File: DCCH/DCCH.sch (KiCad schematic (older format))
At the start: 56 parts, among them J1 Conn_01x02, J2 Conn_01x02, J211 Conn_01x02, J212 Conn_01x02, J221 Conn_01x02, J222 Conn_01x02, J231 Conn_01x02, J232 Conn_01x02, J241 Conn_01x02, J242 Conn_01x02, J3 Conn_02x04_Odd_Even, J4 Conn_02x04_Odd_Even, U11 SN74HC595, U12 SN74HC595, U13 SN74HC595, U14 SN74HC595, U21 SN754410, U22 SN754410, U23 SN754410, U24 SN754410

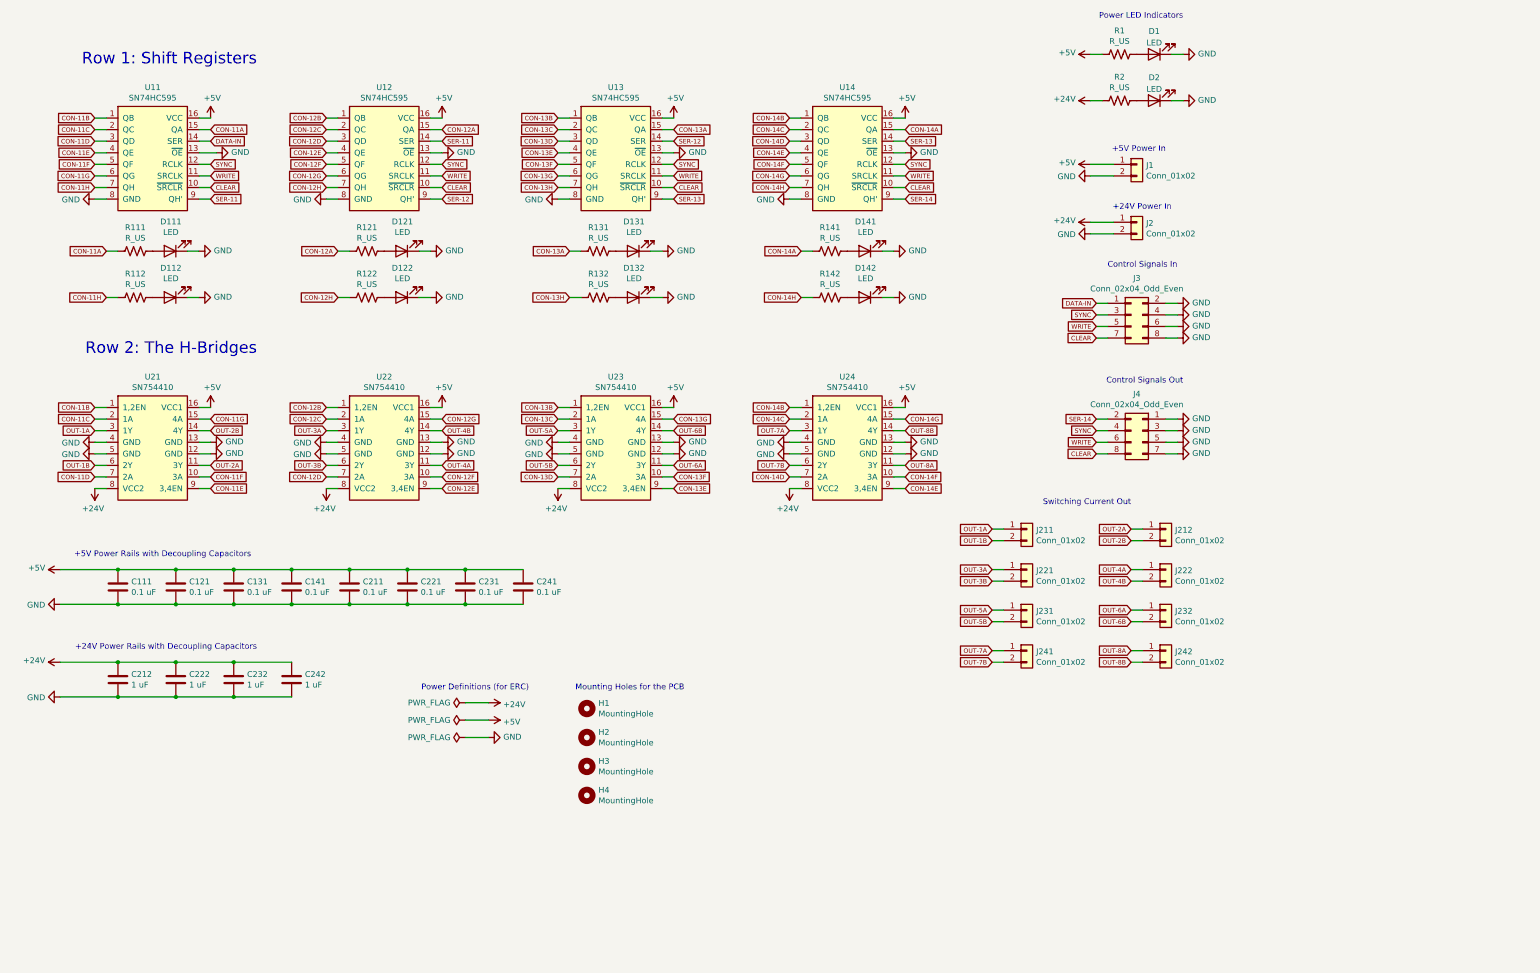
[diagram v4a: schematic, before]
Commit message: Dean completely overhauled the board. Updated board and schematics
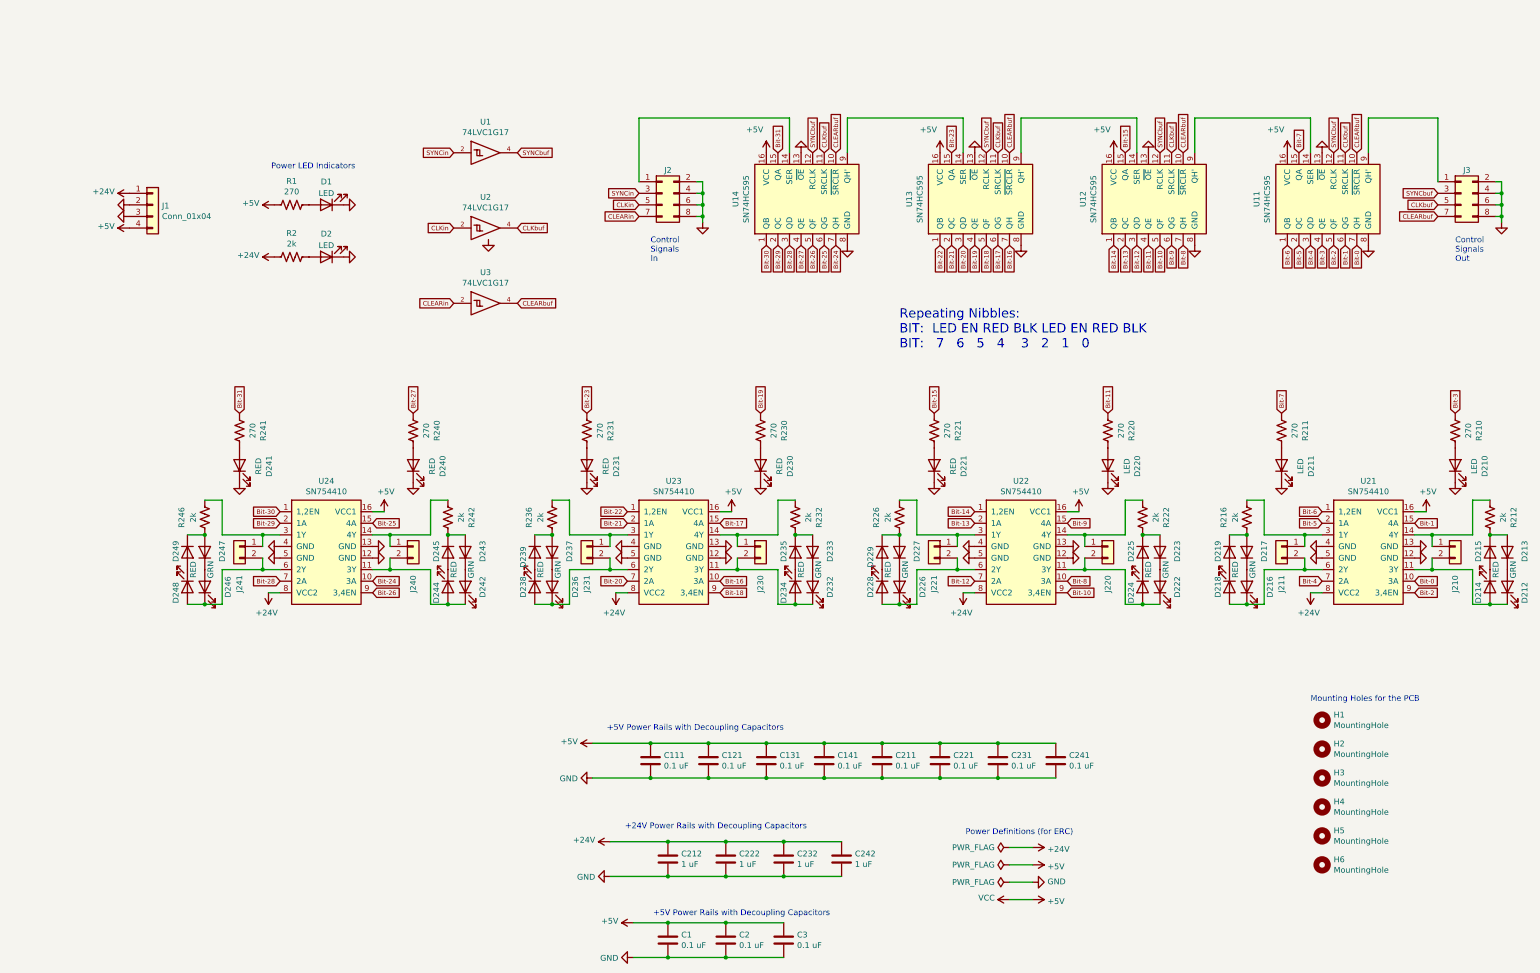
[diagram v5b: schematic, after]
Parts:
- removed J1, J2: Conn_01x02, Connector_Phoenix_MC:PhoenixContact_MC_1,5_2-GF-3.5_1x02_P3.50mm_Horizontal_ThreadedFlange_MountHole, symbol Connector_Generic:Conn_01x02
- added C1, C2, C3: 0.1 uF, Capacitor_SMD:C_0805_2012Metric, symbol Device:C
- added D212, D216, D222, D226, D232, D236, D242, D246: GRN, LED_SMD:LED_0805_2012Metric, symbol Device:LED
- added D213, D215, D217, D219, D223, D225, D227, D229, D233, D235, D237, D239, D243, D245, D247, D249: 1N4148W, Diode_SMD:D_SOD-123, symbol Diode:1N4148W
- added D214, D218, D224, D228, D234, D238, D244, D248: RED, LED_SMD:LED_0805_2012Metric, symbol Device:LED
- added H5, H6: MountingHole, MountingHole:MountingHole_3.5mm, symbol Mechanical:MountingHole
- added J1: Conn_01x04, Connector_Phoenix_MC:PhoenixContact_MC_1,5_4-GF-3.5_1x04_P3.50mm_Horizontal_ThreadedFlange_MountHole, symbol Connector_Generic:Conn_01x04
- added R212, R216, R222, R226, R232, R236, R242, R246: 2k, Resistor_SMD:R_0805_2012Metric, symbol Device:R_US
- added U1, U2, U3: 74LVC1G17, Package_TO_SOT_SMD:SOT-23-5_HandSoldering, symbol 74xGxx:74LVC1G17
- D221: renamed from D131; value LED -> RED
- D230: renamed from D122; value LED -> RED
- D231: renamed from D121; value LED -> RED
- D240: renamed from D112; value LED -> RED
- D241: renamed from D111; value LED -> RED
- J2: renamed from J3; footprint Connector_PinHeader_2.54mm:PinHeader_2x04_P2.54mm_Vertical -> Connector_IDC:IDC-Header_2x04_P2.54mm_Vertical
- J3: renamed from J4; footprint Connector_PinHeader_2.54mm:PinHeader_2x04_P2.54mm_Vertical -> Connector_IDC:IDC-Header_2x04_P2.54mm_Vertical
- R1: value R_US -> 270
- R2: value R_US -> 2k
- R210: renamed from R142; value R_US -> 270
- R211: renamed from R141; value R_US -> 270
- R220: renamed from R132; value R_US -> 270
- R221: renamed from R131; value R_US -> 270
- R230: renamed from R122; value R_US -> 270
- R231: renamed from R121; value R_US -> 270
- R240: renamed from R112; value R_US -> 270
- R241: renamed from R111; value R_US -> 270
- renumbered D142 to D210, D141 to D211, D132 to D220, J242 to J210, J241 to J211, J232 to J220, J231 to J221, J222 to J230, J221 to J231, J212 to J240, J211 to J241, U14 to U11, U13 to U12, U12 to U13, U11 to U14, U24 to U21, U23 to U22, U22 to U23, U21 to U24
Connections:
- net +24V: now also J1.1 (Pin_1)
- net +5V: now also C1.1, C2.1, C3.1, J1.4 (Pin_4), U1.5 (VCC), U2.5 (VCC), U3.5 (VCC)
- net GND: now also J3.2 (Pin_2), J3.4 (Pin_4), J3.6 (Pin_6), J3.8 (Pin_8), C1.2, C2.2, C3.2, J1.2 (Pin_2), J1.3 (Pin_3), U1.3 (GND), U2.3 (GND), U3.3 (GND); no longer J3.1 (Pin_1), J3.3 (Pin_3), J3.5 (Pin_5), J3.7 (Pin_7)
- net CLEAR renamed CLEARbuf
- net CLEARbuf: now also J3.7 (Pin_7), U3.4; no longer J2.7 (Pin_7), J3.8 (Pin_8)
- net CON-11A renamed Bit-31
- net CON-11B renamed Bit-30
- net CON-11C renamed Bit-29
- net CON-11D renamed Bit-28
- net CON-11E renamed Bit-26
- net Bit-26: now also U14.5 (QF); no longer U14.4 (QE)
- net CON-11F renamed Bit-24
- net Bit-24: now also U14.7 (QH); no longer U14.5 (QF)
- net CON-11G renamed Bit-25
- net CON-11H renamed Bit-27
- net Bit-27: now also U14.4 (QE); no longer U14.7 (QH)
- net CON-12A renamed Bit-23
- net CON-12B renamed Bit-22
- net CON-12C renamed Bit-21
- net CON-12D renamed Bit-20
- net CON-12E renamed Bit-18
- net Bit-18: now also U13.5 (QF); no longer U13.4 (QE)
- net CON-12F renamed Bit-16
- net Bit-16: now also U13.7 (QH); no longer U13.5 (QF)
- net CON-12G renamed Bit-17
- net CON-12H renamed Bit-19
- net Bit-19: now also U13.4 (QE); no longer U13.7 (QH)
- net CON-13A renamed Bit-15
- net CON-13B renamed Bit-14
- net CON-13C renamed Bit-13
- net CON-13D renamed Bit-12
- net CON-13E renamed Bit-10
- net Bit-10: now also U12.5 (QF); no longer U12.4 (QE)
- net CON-13F renamed Bit-8
- net Bit-8: now also U12.7 (QH); no longer U12.5 (QF)
- net CON-13G renamed Bit-9
- net CON-13H renamed Bit-11
- net Bit-11: now also U12.4 (QE); no longer U12.7 (QH)
- net CON-14A renamed Bit-7
- net CON-14B renamed Bit-6
- net CON-14C renamed Bit-5
- net CON-14D renamed Bit-4
- net CON-14E renamed Bit-2
- net Bit-2: now also U11.5 (QF); no longer U11.4 (QE)
- net CON-14F renamed Bit-0
- net Bit-0: now also U11.7 (QH); no longer U11.5 (QF)
- net CON-14G renamed Bit-1
- net CON-14H renamed Bit-3
- net Bit-3: now also U11.4 (QE); no longer U11.7 (QH)
- net DATA-IN: no longer names the net of J2.1 (Pin_1), U14.14 (SER)
- net OUT-1A: no longer names the net of J241.1 (Pin_1), U24.3 (1Y)
- net OUT-1A: now also R246.2
- net OUT-1B: no longer names the net of J241.2 (Pin_2), U24.6 (2Y)
- net OUT-1B: now also D246.1 (K), D248.2 (A)
- net OUT-2A: no longer names the net of U24.11 (3Y)
- net OUT-2A: now also J240.2 (Pin_2), D242.1 (K), D244.2 (A); no longer J240.1 (Pin_1)
- net OUT-2B: no longer names the net of U24.14 (4Y)
- net OUT-2B: now also J240.1 (Pin_1), R242.2; no longer J240.2 (Pin_2)
- net OUT-3A: no longer names the net of J231.1 (Pin_1), U23.3 (1Y)
- net OUT-3A: now also R236.2
- net OUT-3B: no longer names the net of J231.2 (Pin_2), U23.6 (2Y)
- net OUT-3B: now also D236.1 (K), D238.2 (A)
- net OUT-4A: no longer names the net of U23.11 (3Y)
- net OUT-4A: now also J230.2 (Pin_2), D232.1 (K), D234.2 (A); no longer J230.1 (Pin_1)
- net OUT-4B: no longer names the net of U23.14 (4Y)
- net OUT-4B: now also J230.1 (Pin_1), R232.2; no longer J230.2 (Pin_2)
- net OUT-5A: no longer names the net of J221.1 (Pin_1), U22.3 (1Y)
- net OUT-5A: now also R226.2
- net OUT-5B: no longer names the net of J221.2 (Pin_2), U22.6 (2Y)
- net OUT-5B: now also D226.1 (K), D228.2 (A)
- net OUT-6A: no longer names the net of U22.11 (3Y)
- net OUT-6A: now also J220.2 (Pin_2), D222.1 (K), D224.2 (A); no longer J220.1 (Pin_1)
- net OUT-6B: no longer names the net of U22.14 (4Y)
- net OUT-6B: now also J220.1 (Pin_1), R222.2; no longer J220.2 (Pin_2)
- net OUT-7A: no longer names the net of J211.1 (Pin_1), U21.3 (1Y)
- net OUT-7A: now also R216.2
- net OUT-7B: no longer names the net of J211.2 (Pin_2), U21.6 (2Y)
- net OUT-7B: now also D216.1 (K), D218.2 (A)
- net OUT-8A: no longer names the net of U21.11 (3Y)
- net OUT-8A: now also J210.2 (Pin_2), D212.1 (K), D214.2 (A); no longer J210.1 (Pin_1)
- net OUT-8B: no longer names the net of U21.14 (4Y)
- net OUT-8B: now also J210.1 (Pin_1), R212.2; no longer J210.2 (Pin_2)
- net SER-11: no longer names the net of U13.14 (SER), U14.9 (QH')
- net SER-12: no longer names the net of U12.14 (SER), U13.9 (QH')
- net SER-13: no longer names the net of U11.14 (SER), U12.9 (QH')
- net SER-14: no longer names the net of U11.9 (QH')
- net SER-14: now also J3.1 (Pin_1); no longer J3.2 (Pin_2)
- net SYNC renamed SYNCbuf
- net SYNCbuf: now also J3.3 (Pin_3), U1.4; no longer J2.3 (Pin_3), J3.4 (Pin_4)
- net WRITE renamed CLKbuf
- net CLKbuf: now also J3.5 (Pin_5), U2.4; no longer J2.5 (Pin_5), J3.6 (Pin_6)
- new net: D236.2 (A), D237.1 (K)
- new net: D237.2 (A), D239.1 (K), R236.1
- new net: D238.1 (K), D239.2 (A)
- new net: D242.2 (A), D243.1 (K)
- new net: D243.2 (A), D245.1 (K), R242.1
- new net: D244.1 (K), D245.2 (A)
- new net: D226.2 (A), D227.1 (K)
- new net: D227.2 (A), D229.1 (K), R226.1
- new net: D228.1 (K), D229.2 (A)
- new net: D232.2 (A), D233.1 (K)
- new net: D233.2 (A), D235.1 (K), R232.1
- new net: D234.1 (K), D235.2 (A)
- new net: D216.2 (A), D217.1 (K)
- new net: D217.2 (A), D219.1 (K), R216.1
- new net: D218.1 (K), D219.2 (A)
- new net: D222.2 (A), D223.1 (K)
- new net: D223.2 (A), D225.1 (K), R222.1
- new net: D224.1 (K), D225.2 (A)
- new net: D212.2 (A), D213.1 (K)
- new net: D213.2 (A), D215.1 (K), R212.1
- new net: D214.1 (K), D215.2 (A)
- new net: D246.2 (A), D247.1 (K)
- new net: D247.2 (A), D249.1 (K), R246.1
- new net: D248.1 (K), D249.2 (A)
- new net CLEARin: J2.7 (Pin_7), U3.2
- new net CLKin: J2.5 (Pin_5), U2.2
- new net SYNCin: J2.3 (Pin_3), U1.2
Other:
- note added: "Control\nSignals\nIn"
- note added: "Control\nSignals\nOut"
- note added: "Repeating Nibbles:\nBIT: LED EN RED BLK LED EN RED BLK\nBIT: 7 6 5 4 3 2 1 0"
- note removed: "+24V Power In\n"
- note removed: "+5V Power In\n"
- note removed: "Control Signals In"
- note removed: "Control Signals Out"
- note removed: "Row 1: Shift Registers"
- note removed: "Row 2: The H-Bridges"
- note removed: "Switching Current Out"
- moved on the sheet: C111, C121, C131, C141, C211, C212, C221, C222, C231, C232, C241, C242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
